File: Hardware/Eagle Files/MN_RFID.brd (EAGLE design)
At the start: 100 x 80 mm, 23 parts, among them IC1 74HCT125N, J1 USB_B_PTH, U1 ARGON

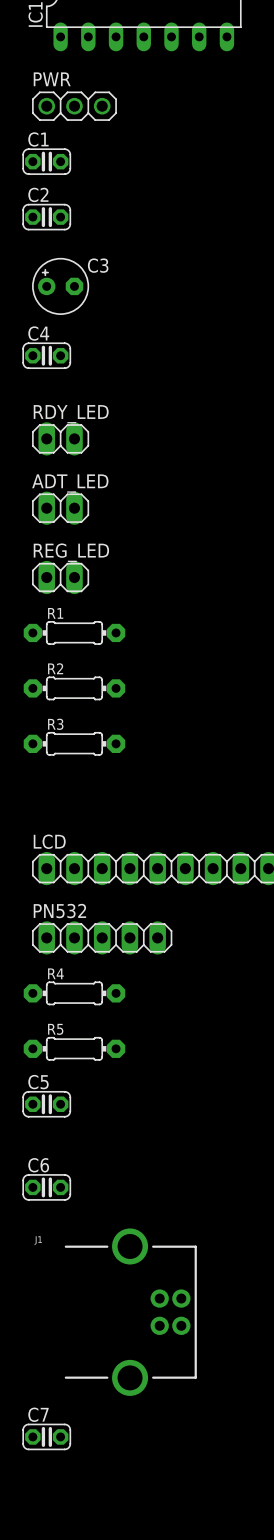
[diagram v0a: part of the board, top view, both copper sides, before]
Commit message: Updated Schematic
Updated schematic per testing breadboard at MN 8/07/19.  Decided to power from Argon and remove external 5v USB connector, 3.3v power converter, and 100 uF cap.  5v supplied from Argon via VUSB pin.  3.3v supplied from Argon via 3.3v pin.  Also added 5.6Kohm pulldown on D4 to prevent buzzer from going off while Argon sets up.
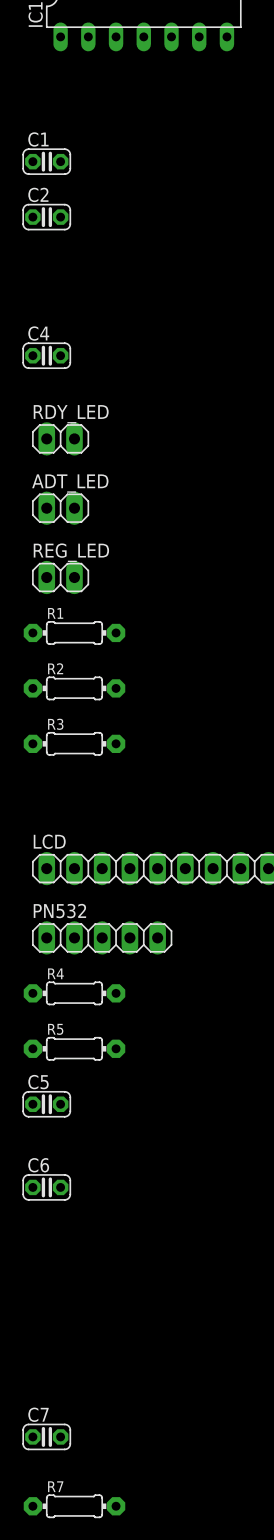
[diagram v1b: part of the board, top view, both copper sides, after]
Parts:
- removed C3: 100uF, adafruit:E2,5-5
- removed J1: USB_B_PTH, SparkFun-Connectors:USB-B-PTH
- removed PWR: (no value), adafruit:1X03
- added R7: 5.6k, adafruit:0204/7
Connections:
- removed net N$19: IC1.2, U1.19
- removed net VUSB: U1.26
- new net N$22: IC1.2, R7.1, U1.19
- net 3.3V: no longer PWR.2
- net 5V: now also U1.26; no longer C3.+, J1.VBUS, PWR.1
- net GND: now also R7.2; no longer C3.-, J1.GND, J1.SHLD1, J1.SHLD2, PWR.3
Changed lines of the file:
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@@
 <attribute name="VALUE" x="-33.401" y="-23.495" size="1.27" layer="27" ratio="10"/>
-</element>
-<element name="PWR" library="adafruit" library_urn="urn:adsk.eagle:library:420" package="1X03" package3d_urn="urn:adsk.eagle:package:6240710/1" value="" x="-33.02" y="-33.02" smashed="yes">
-<attribute name="NAME" x="-36.9062" y="-31.1912" size="1.27" layer="25" ratio="10"/>
-<attribute name="VALUE" x="-36.83" y="-36.195" size="1.27" layer="27"/>
 </element>
 <element name="C1" library="adafruit" library_urn="urn:adsk.eagle:library:420" package="C025-024X044" package3d_urn="urn:adsk.eagle:package:6240324/1" value="0.1uF" x="-35.56" y="-38.1" smashed="yes">
@@
 <attribute name="VALUE" x="-37.338" y="-45.847" size="1.27" layer="27" ratio="10"/>
 </element>
-<element name="C3" library="adafruit" library_urn="urn:adsk.eagle:library:420" package="E2,5-5" package3d_urn="urn:adsk.eagle:package:6240498/1" value="100uF" x="-34.29" y="-49.53" smashed="yes">
-<attribute name="NAME" x="-31.877" y="-48.26" size="1.27" layer="25" ratio="10"/>
-<attribute name="VALUE" x="-31.877" y="-51.943" size="1.27" layer="27" ratio="10"/>
-</element>
 <element name="C4" library="adafruit" library_urn="urn:adsk.eagle:library:420" package="C025-024X044" package3d_urn="urn:adsk.eagle:package:6240324/1" value="0.1uF" x="-35.56" y="-55.88" smashed="yes">
 <attribute name="NAME" x="-37.338" y="-54.483" size="1.27" layer="25" ratio="10"/>
@@
 <attribute name="VALUE" x="11.9634" y="10.033" size="1.27" layer="27" ratio="10"/>
 </element>
-<element name="J1" library="SparkFun-Connectors" library_urn="urn:adsk.eagle:library:513" package="USB-B-PTH" package3d_urn="urn:adsk.eagle:package:38301/1" value="USB_B_PTH" x="-29.21" y="-143.51" smashed="yes">
-<attribute name="NAME" x="-36.64" y="-137.16" size="0.6096" layer="25" font="vector" ratio="20"/>
-<attribute name="PROD_ID" value="CONN-08278" x="-29.21" y="-143.51" size="1.778" layer="27" display="off"/>
-<attribute name="SF_ID" value="PRT-00139" x="-29.21" y="-143.51" size="1.778" layer="27" display="off"/>
-<attribute name="VALUE" x="-36.64" y="-149.86" size="0.6096" layer="27" font="vector" ratio="20" align="top-left"/>
-</element>
 <element name="C7" library="adafruit" library_urn="urn:adsk.eagle:library:420" package="C025-024X044" package3d_urn="urn:adsk.eagle:package:6240324/1" value="0.1uF" x="-35.56" y="-154.94" smashed="yes">
 <attribute name="NAME" x="-37.338" y="-153.543" size="1.27" layer="25" ratio="10"/>
 <attribute name="VALUE" x="-37.338" y="-157.607" size="1.27" layer="27" ratio="10"/>
+</element>
+<element name="R7" library="adafruit" library_urn="urn:adsk.eagle:library:420" package="0204/7" package3d_urn="urn:adsk.eagle:package:6240596/1" value="5.6k" x="-33.02" y="-161.29" smashed="yes">
+<attribute name="NAME" x="-35.56" y="-159.9946" size="0.9906" layer="25" ratio="12"/>
+<attribute name="VALUE" x="-34.6456" y="-161.7726" size="0.9906" layer="27" ratio="12"/>
 </element>
 </elements>
@@
 <contactref element="IC1" pad="1"/>
 <contactref element="SG1" pad="-"/>
-<contactref element="PWR" pad="3"/>
 <contactref element="U1" pad="27"/>
 <contactref element="RDY_LED" pad="2"/>
@@
 <contactref element="PN532" pad="1"/>
 <contactref element="R6" pad="A"/>
-<contactref element="J1" pad="GND"/>
-<contactref element="J1" pad="SHLD2"/>
-<contactref element="J1" pad="SHLD1"/>
-<contactref element="C3" pad="-"/>
 <contactref element="C1" pad="2"/>
 <contactref element="C6" pad="2"/>
@@
 <contactref element="C4" pad="2"/>
 <contactref element="C5" pad="2"/>
-<wire x1="-27.9278" y1="-149.5298" x2="-34.29" y2="-154.94" width="0" layer="19" extent="1-1"/>
-<wire x1="-25.21" y1="-144.76" x2="-27.9278" y2="-149.5298" width="0" layer="19" extent="1-1"/>
-<wire x1="-27.9278" y1="-137.4902" x2="-25.21" y2="-144.76" width="0" layer="19" extent="1-1"/>
-<wire x1="-34.29" y1="-132.08" x2="-27.9278" y2="-137.4902" width="0" layer="19" extent="1-1"/>
+<contactref element="R7" pad="2"/>
+<wire x1="-29.21" y1="-161.29" x2="-34.29" y2="-154.94" width="0" layer="19" extent="1-1"/>
+<wire x1="-34.29" y1="-132.08" x2="-34.29" y2="-154.94" width="0" layer="19" extent="1-1"/>
 <wire x1="-34.29" y1="-124.46" x2="-34.29" y2="-132.08" width="0" layer="19" extent="1-1"/>
 <wire x1="-35.56" y1="-109.22" x2="-34.29" y2="-124.46" width="0" layer="19" extent="1-1"/>
@@
 <wire x1="-33.02" y1="-63.5" x2="-33.02" y2="-69.85" width="0" layer="19" extent="1-1"/>
 <wire x1="-34.29" y1="-55.88" x2="-33.02" y2="-63.5" width="0" layer="19" extent="1-1"/>
-<wire x1="-33.02" y1="-49.53" x2="-34.29" y2="-55.88" width="0" layer="19" extent="1-1"/>
-<wire x1="-34.29" y1="-43.18" x2="-33.02" y2="-49.53" width="0" layer="19" extent="1-1"/>
+<wire x1="-34.29" y1="-43.18" x2="-34.29" y2="-55.88" width="0" layer="19" extent="1-1"/>
 <wire x1="-34.29" y1="-38.1" x2="-34.29" y2="-43.18" width="0" layer="19" extent="1-1"/>
-<wire x1="-30.48" y1="-33.02" x2="-34.29" y2="-38.1" width="0" layer="19" extent="1-1"/>
-<wire x1="-34.29" y1="-26.67" x2="-30.48" y2="-33.02" width="0" layer="19" extent="1-1"/>
-<wire x1="-26.67" y1="-26.67" x2="-30.48" y2="-33.02" width="0" layer="19" extent="1-1"/>
+<wire x1="-34.29" y1="-26.67" x2="-34.29" y2="-38.1" width="0" layer="19" extent="1-1"/>
+<wire x1="-26.67" y1="-26.67" x2="-34.29" y2="-26.67" width="0" layer="19" extent="1-1"/>
 <wire x1="-19.05" y1="-26.67" x2="-26.67" y2="-26.67" width="0" layer="19" extent="1-1"/>
 <wire x1="-31.75" y1="-19.05" x2="-34.29" y2="-26.67" width="0" layer="19" extent="1-1"/>
@@
 <wire x1="17.7546" y1="15.24" x2="-15.24" y2="36.83" width="0" layer="19" extent="1-1"/>
 </signal>
-<signal name="VUSB">
-<contactref element="U1" pad="26"/>
-</signal>
 <signal name="LI+">
 <contactref element="U1" pad="28"/>
@@
 <signal name="5V">
 <contactref element="IC1" pad="14"/>
-<contactref element="PWR" pad="1"/>
 <contactref element="C1" pad="1"/>
-<contactref element="C3" pad="+"/>
 <contactref element="PN532" pad="2"/>
 <contactref element="C6" pad="1"/>
-<contactref element="J1" pad="VBUS"/>
 <contactref element="C7" pad="1"/>
-<wire x1="-23.2288" y1="-144.76" x2="-36.83" y2="-154.94" width="0" layer="19" extent="1-1"/>
-<wire x1="-36.83" y1="-132.08" x2="-23.2288" y2="-144.76" width="0" layer="19" extent="1-1"/>
+<contactref element="U1" pad="26"/>
+<wire x1="-36.83" y1="-132.08" x2="-36.83" y2="-154.94" width="0" layer="19" extent="1-1"/>
 <wire x1="-33.02" y1="-109.22" x2="-36.83" y2="-132.08" width="0" layer="19" extent="1-1"/>
-<wire x1="-35.56" y1="-49.53" x2="-33.02" y2="-109.22" width="0" layer="19" extent="1-1"/>
-<wire x1="-36.83" y1="-38.1" x2="-35.56" y2="-49.53" width="0" layer="19" extent="1-1"/>
-<wire x1="-35.56" y1="-33.02" x2="-36.83" y2="-38.1" width="0" layer="19" extent="1-1"/>
-<wire x1="-34.29" y1="-19.05" x2="-35.56" y2="-33.02" width="0" layer="19" extent="1-1"/>
+<wire x1="-36.83" y1="-38.1" x2="-33.02" y2="-109.22" width="0" layer="19" extent="1-1"/>
+<wire x1="-34.29" y1="-19.05" x2="-36.83" y2="-38.1" width="0" layer="19" extent="1-1"/>
+<wire x1="-15.24" y1="34.29" x2="-34.29" y2="-19.05" width="0" layer="19" extent="1-1"/>
 </signal>
 <signal name="3.3V">
-<contactref element="PWR" pad="2"/>
 <contactref element="U1" pad="2"/>
-<contactref element="C2" pad="1"/>
-<contactref element="C4" pad="1"/>
 <contactref element="LCD" pad="2"/>
 <contactref element="LCD" pad="15"/>
 <contactref element="R5" pad="2"/>
 <contactref element="R4" pad="2"/>
+<contactref element="R6" pad="E"/>
+<contactref element="C2" pad="1"/>
+<contactref element="C4" pad="1"/>
 <contactref element="C5" pad="1"/>
-<contactref element="R6" pad="E"/>
 <wire x1="-29.21" y1="-119.38" x2="-36.83" y2="-124.46" width="0" layer="19" extent="1-1"/>
 <wire x1="-29.21" y1="-114.3" x2="-29.21" y2="-119.38" width="0" layer="19" extent="1-1"/>
@@
 <wire x1="-36.83" y1="-55.88" x2="-33.02" y2="-102.87" width="0" layer="19" extent="1-1"/>
 <wire x1="-36.83" y1="-43.18" x2="-36.83" y2="-55.88" width="0" layer="19" extent="1-1"/>
-<wire x1="-33.02" y1="-33.02" x2="-36.83" y2="-43.18" width="0" layer="19" extent="1-1"/>
-<wire x1="12.7254" y1="15.24" x2="-33.02" y2="-33.02" width="0" layer="19" extent="1-1"/>
+<wire x1="12.7254" y1="15.24" x2="-36.83" y2="-43.18" width="0" layer="19" extent="1-1"/>
 <wire x1="-35.56" y1="46.99" x2="12.7254" y2="15.24" width="0" layer="19" extent="1-1"/>
 </signal>
@@
 <wire x1="15.24" y1="12.7" x2="-30.48" y2="-102.87" width="0" layer="19" extent="1-1"/>
 </signal>
-<signal name="N$19">
-<contactref element="U1" pad="19"/>
-<contactref element="IC1" pad="2"/>
-<wire x1="-15.24" y1="16.51" x2="-31.75" y2="-26.67" width="0" layer="19" extent="1-1"/>
-</signal>
 <signal name="N$20">
 <contactref element="U1" pad="21"/>
@@
 <wire x1="-35.56" y1="26.67" x2="-29.21" y2="-19.05" width="0" layer="19" extent="1-1"/>
 </signal>
+<signal name="N$22">
+<contactref element="U1" pad="19"/>
+<contactref element="IC1" pad="2"/>
+<contactref element="R7" pad="1"/>
+<wire x1="-31.75" y1="-26.67" x2="-36.83" y2="-161.29" width="0" layer="19" extent="1-1"/>
+<wire x1="-15.24" y1="16.51" x2="-31.75" y2="-26.67" width="0" layer="19" extent="1-1"/>
+</signal>
 </signals>

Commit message: PCB Parts PLacement
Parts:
- moved R7 225.8 mm to (33.0, 54.6), turned to 180 degrees
- moved C7 216.3 mm to (83.8, 25.4)
- moved R5 208.2 mm to (81.3, 54.6), turned to 90 degrees
- moved R4 206.8 mm to (86.4, 54.6), turned to 270 degrees
- moved C6 196.0 mm to (47.0, 45.7)
- moved PN532 187.0 mm to (86.4, 36.8), turned to 90 degrees
- moved C5 183.5 mm to (47.0, 39.4)
- moved C2 164.4 mm to (82.5, 71.1), turned to 180 degrees
- moved R1 147.8 mm to (38.1, 48.3), flipped to the bottom, turned to 270 degrees
- moved LCD 146.5 mm to (64.8, 19.1)
- moved R2 143.3 mm to (38.1, 38.1), turned to 270 degrees
- moved R3 139.0 mm to (38.1, 27.9), turned to 270 degrees
- moved C1 138.2 mm to (45.7, 73.7), turned to 180 degrees
- moved RDY_LED 126.3 mm to (29.2, 45.7), turned to 90 degrees
- moved ADT_LED 123.1 mm to (29.2, 35.6), turned to 90 degrees
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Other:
- board size 100 x 80 mm -> 72.1 x 64.8 mm

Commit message: Update MN_RFID.brd
Jiggled around the layout a little.
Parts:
- moved C2 47.1 mm to (86.4, 24.1), turned to 0 degrees
- moved C7 30.5 mm to (85.1, 55.9)
- moved R5 10.5 mm to (83.8, 64.8)
- moved R4 10.2 mm to (87.6, 64.8)
- moved PN532 6.48 mm to (87.6, 43.2), turned to 270 degrees
- moved R3 5.39 mm to (34.3, 24.1)
- moved R2 4.58 mm to (34.3, 35.6)
- moved R1 4.02 mm to (34.3, 47.0)
- moved REG_LED 1.80 mm to (27.9, 26.7)
- moved C1 1.27 mm to (47.0, 73.7)
- moved R7 1.27 mm to (33.0, 55.9)
- moved U1 1.27 mm to (55.9, 29.2)
- moved ADT_LED 1.27 mm to (27.9, 35.6)
- moved RDY_LED 1.27 mm to (27.9, 45.7)
- moved SG1 1.27 mm to (31.8, 67.3)

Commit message: Updated schematic
Changed pull-up/down resistors from 5.6K to 4.7K -- more common value.
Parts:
- R4, R5, R7: value 5.6k -> 4.7K
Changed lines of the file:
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@@
 <attribute name="VALUE" x="84.455" y="49.53" size="1.27" layer="27" rot="R270"/>
 </element>
-<element name="R4" library="adafruit" library_urn="urn:adsk.eagle:library:420" package="0204/7" package3d_urn="urn:adsk.eagle:package:6240596/1" value="5.6k" x="87.63" y="64.77" smashed="yes" rot="R270">
+<element name="R4" library="adafruit" library_urn="urn:adsk.eagle:library:420" package="0204/7" package3d_urn="urn:adsk.eagle:package:6240596/1" value="4.7K" x="87.63" y="64.77" smashed="yes" rot="R270">
 <attribute name="NAME" x="88.9254" y="67.31" size="0.9906" layer="25" ratio="12" rot="R270"/>
 <attribute name="VALUE" x="87.1474" y="66.3956" size="0.9906" layer="27" ratio="12" rot="R270"/>
 </element>
-<element name="R5" library="adafruit" library_urn="urn:adsk.eagle:library:420" package="0204/7" package3d_urn="urn:adsk.eagle:package:6240596/1" value="5.6k" x="83.82" y="64.77" smashed="yes" rot="R90">
+<element name="R5" library="adafruit" library_urn="urn:adsk.eagle:library:420" package="0204/7" package3d_urn="urn:adsk.eagle:package:6240596/1" value="4.7K" x="83.82" y="64.77" smashed="yes" rot="R90">
 <attribute name="NAME" x="82.5246" y="62.23" size="0.9906" layer="25" ratio="12" rot="R90"/>
 <attribute name="VALUE" x="84.3026" y="63.1444" size="0.9906" layer="27" ratio="12" rot="R90"/>
@@
 <attribute name="VALUE" x="83.312" y="53.213" size="1.27" layer="27" ratio="10"/>
 </element>
-<element name="R7" library="adafruit" library_urn="urn:adsk.eagle:library:420" package="0204/7" package3d_urn="urn:adsk.eagle:package:6240596/1" value="5.6k" x="33.02" y="55.88" smashed="yes" rot="R180">
+<element name="R7" library="adafruit" library_urn="urn:adsk.eagle:library:420" package="0204/7" package3d_urn="urn:adsk.eagle:package:6240596/1" value="4.7K" x="33.02" y="55.88" smashed="yes" rot="R180">
 <attribute name="NAME" x="35.56" y="54.5846" size="0.9906" layer="25" ratio="12" rot="R180"/>
 <attribute name="VALUE" x="34.6456" y="56.3626" size="0.9906" layer="27" ratio="12" rot="R180"/>

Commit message: PCB Finalization
Added expansion connector and board name.  Routed and coppoer pour.  Annotated the top silkscreen layer for connection information.
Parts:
- added XPND: (no value), adafruit:1X08-BIG
- moved R1 1.27 mm to (33.0, 47.0)
- moved R2 1.27 mm to (33.0, 35.6)
- moved R3 1.27 mm to (33.0, 24.1)
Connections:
- new net N$19: U1.25, XPND.3
- new net N$23: U1.13, XPND.4
- new net N$24: U1.12, XPND.5
- new net N$25: U1.11, XPND.6
- net 3.3V: now also XPND.2
- net 5V: now also XPND.1
- net GND: now also XPND.7, XPND.8
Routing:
- net GND: track 0.00 -> 241.9 mm
- net 3.3V: track 0.00 -> 152.7 mm
- net 5V: track 0.00 -> 106.4 mm
- net N$22: track 0.00 -> 71.1 mm
- net N$11: track 0.00 -> 69.5 mm
- net N$10: track 0.00 -> 64.0 mm
- net N$19: track 0.00 -> 56.8 mm
- net N$9: track 0.00 -> 54.6 mm
- net N$8: track 0.00 -> 47.7 mm
- net N$14: track 0.00 -> 46.3 mm
- net N$4: track 0.00 -> 43.3 mm
- net N$20: track 0.00 -> 39.0 mm
- net N$13: track 0.00 -> 36.2 mm
- net N$12: track 0.00 -> 35.5 mm
- net N$16: track 0.00 -> 31.7 mm
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- added copper zone on layer 1, net GND
- added copper zone on layer 16, net GND
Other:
- board text added: "(c) 2019, Team Practical Projects"
- board text added: "+"
- board text added: "+3.3v"
- board text added: "+5v"
- board text added: "-"
- board text added: "1"
- board text added: "10"
- board text added: "11"
- board text added: "12"
- board text added: "13"
- board text added: "14"
- board text added: "15"
- board text added: "16"
- board text added: "2"
- board text added: "3"
- board text added: "4"
- board text added: "5"
- board text added: "6"
- board text added: "7"
- board text added: "8"
- board text added: "9"
- board text added: "D8"
- board text added: "GND"
- board text added: "IRQ"
- board text added: "MISO"
- board text added: "MOSI"
- board text added: "Particle Argon/Xenon"
- board text added: "RFID CARD PROCESSOR"
- board text added: "SCL"
- board text added: "SDA"
